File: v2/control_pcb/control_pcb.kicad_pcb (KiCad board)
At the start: 2 copper layers, 177 x 105.5 mm, 72 parts, among them J1 Raspberry_Pi_2_3, J10 8P8C_Shielded, J11 Screw_Terminal_01x02, J12 Screw_Terminal_01x02, J13 Screw_Terminal_01x02, J14 Conn_02x02_Top_Bottom, J15 Conn_02x02_Top_Bottom, J2 8P8C_Shielded, J3 Conn_01x08, J4 Conn_01x08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

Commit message: Doing more things
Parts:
- removed R20: 4k, Resistor_THT:R_Axial_DIN0207_L6.3mm_D2.5mm_P10.16mm_Horizontal
- removed U8: LM404C30ILPR, Package_TO_SOT_THT:TO-92_Inline
- added C7: 0.1uF, Capacitor_THT:C_Rect_L4.6mm_W2.0mm_P2.50mm_MKS02_FKP02, F.Cu at (120.5, 108.2)
- added G***: LOGO, LOGO, F.Cu at (173.5, 100.0)
- added R24: 10kR, Resistor_THT:R_Axial_DIN0207_L6.3mm_D2.5mm_P10.16mm_Horizontal, F.Cu at (138.1, 124.5)
- added R25: 10kR, Resistor_THT:R_Axial_DIN0207_L6.3mm_D2.5mm_P10.16mm_Horizontal, F.Cu at (138.1, 121.5)
- R17: value 904R -> 4k
- U9: value ~ -> ADS7138IRTER
- moved R23 319.3 mm to (228.0, 77.4), turned to -90 degrees
- moved H4 316.1 mm to (236.0, 33.0)
- moved H3 315.7 mm to (236.0, 129.0)
- moved R22 314.3 mm to (225.0, 87.6), turned to 90 degrees
- moved R19 305.7 mm to (218.5, 99.6), turned to 90 degrees
- moved U9 303.5 mm to (216.1, 81.6)
- moved R21 303.2 mm to (215.0, 89.4), turned to -90 degrees
- moved R18 298.9 mm to (211.6, 89.4), turned to -90 degrees
- moved R17 279.3 mm to (208.0, 99.6), turned to 90 degrees
- moved J4 252.2 mm to (228.7, 31.0), turned to -90 degrees
- moved C11 243.6 mm to (215.0, 38.5), turned to 180 degrees
- moved C12 242.2 mm to (214.8, 46.5), turned to 180 degrees
- moved C6 240.4 mm to (220.5, 80.8), turned to -90 degrees
- moved C2 232.5 mm to (204.5, 58.5), turned to 90 degrees
- moved C3 189.5 mm to (118.0, 114.8)
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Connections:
- C5 pad 1: +3.3V -> 3V3_PICO
- R17 pad 1: +5V -> +24V
- R17 pad 2: Net-(U3-VREF) -> Net-(U9-AIN6)
- R18 pad 1: +5V -> Net-(U9-AIN6)
- R18 pad 2: Net-(U9-AIN4) -> GND
- U10 pad 1: +5V -> +12V
- U10 pad 2: +5V -> +12V
- U11 pad 1: +12V -> +5V
- U11 pad 2: +12V -> +5V
- U3 pad 35: Net-(U3-VREF) -> unconnected-(U3-VREF-Pad35)
- U6 pad 1: +5V -> +12V
- U6 pad 2: +5V -> +12V
- U7 pad 1: +12V -> +5V
- U7 pad 2: +12V -> +5V
- U9 pad 3: Net-(U9-AIN4) -> +5V
- U9 pad 5: unconnected-(U9-AIN6-Pad5) -> Net-(U9-AIN6)
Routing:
- net +24V: track 0.00 -> 288.1 mm, vias 0 -> 46
- net LIMIT_SW_RR: track 0.00 -> 259.1 mm, vias 0 -> 6
- net LIMIT_SW_RL: track 0.00 -> 246.9 mm, vias 0 -> 3
- net Net-(J9-Pin_7): track 0.00 -> 213.7 mm
- net +12V: track 0.00 -> 208.0 mm, vias 0 -> 20
- net SDA: track 0.00 -> 207.3 mm, vias 0 -> 4
- net SCL: track 0.00 -> 205.6 mm, vias 0 -> 4
- net Net-(J9-Pin_5): track 0.00 -> 204.2 mm
- net Net-(J9-Pin_3): track 0.00 -> 194.8 mm
- net Net-(J9-Pin_1): track 0.00 -> 185.3 mm
- net Net-(U7-VOUT): track 0.00 -> 164.3 mm, vias 0 -> 4
- net Net-(U6-VOUT): track 0.00 -> 164.0 mm, vias 0 -> 4
- net +5V: track 3.00 -> 150.6 mm, vias 0 -> 34
- net LED1: track 0.00 -> 94.9 mm, vias 0 -> 2
- net LED2: track 0.00 -> 85.7 mm, vias 0 -> 2
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- added copper zone on B.Cu, net +12V
- added copper zone on F.Cu, net +12V
- added copper zone on B.Cu, net +24V
- added copper zone on F.Cu, net +24V
- added copper zone on F.Cu, net +5V
- added copper zone on B.Cu, net GND
- added copper zone on F.Cu, net GND
- added copper zone on F.Cu, net Net-(J14-Pin_3)
- added copper zone on F.Cu, net Net-(J14-Pin_4)
- added copper zone on F.Cu, net Net-(J15-Pin_3)
- added copper zone on F.Cu, net Net-(J15-Pin_4)
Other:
- board size 177 x 105.5 mm -> 177 x 106 mm
- board text added: "+12V"
- board text added: "+24V"
- board text added: "+5V"
- board text added: "-"
- board text added: "24V"
- board text added: "ALARM+"
- board text added: "ALARM-"
- board text added: "BOT-HOVEN"
- board text added: "CONTROL PCB VERSION 2"
- board text added: "DESIGNED BY J. PETERSEN"
- board text added: "DIR+"
- board text added: "DIR-"
- board text added: "DSCL+"
- board text added: "DSCL-"
- board text added: "DSDA+"
- board text added: "DSDA-"
- board text added: "ENA+"
- board text added: "ENA-"
- board text added: "GND"
- board text added: "J. PETERSEN A. POTENZA A. ZAKY"
- board text added: "PUL+"
- board text added: "RASPBERRY PI PICO"
- board text added: "SCL"
- board text added: "SDA"
- board text added: "T. DOBROWNEY E. EVANIUK C. KOLASKI"
- board text added: "|-GND-|"

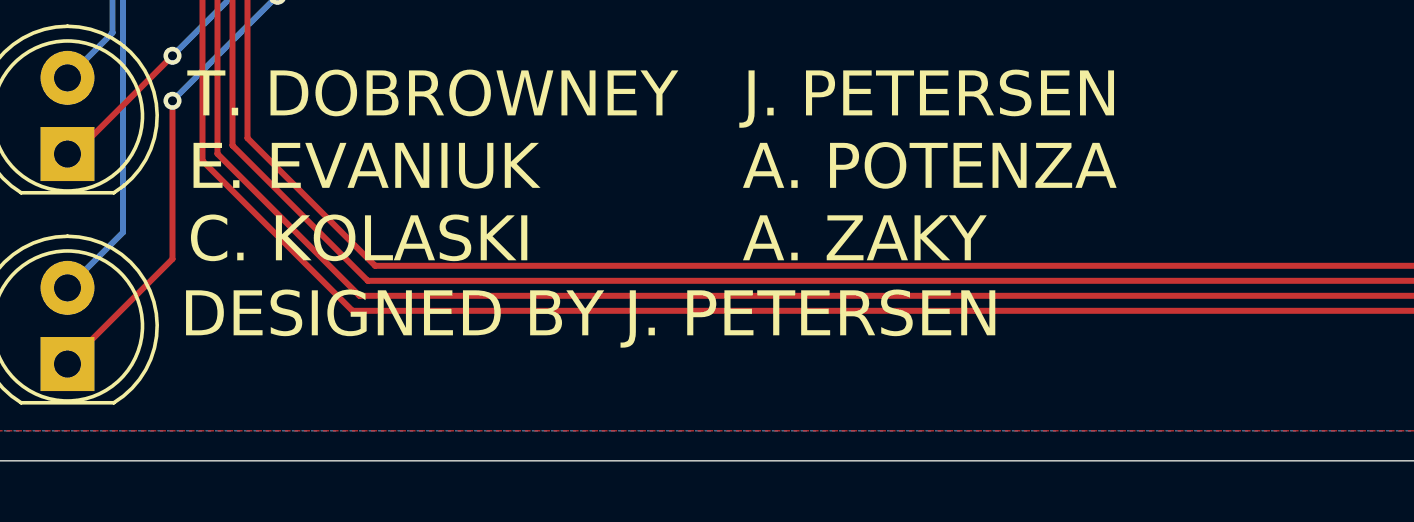
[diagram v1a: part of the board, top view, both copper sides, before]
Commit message: Version 2 As-Ordered commit
Minor changes to polish things up.
Version 2 is a major revision from the last revision, version 1. There are now 10 servo channels in addition to the 5 solenoid channels, and ADC feedback for those servos.
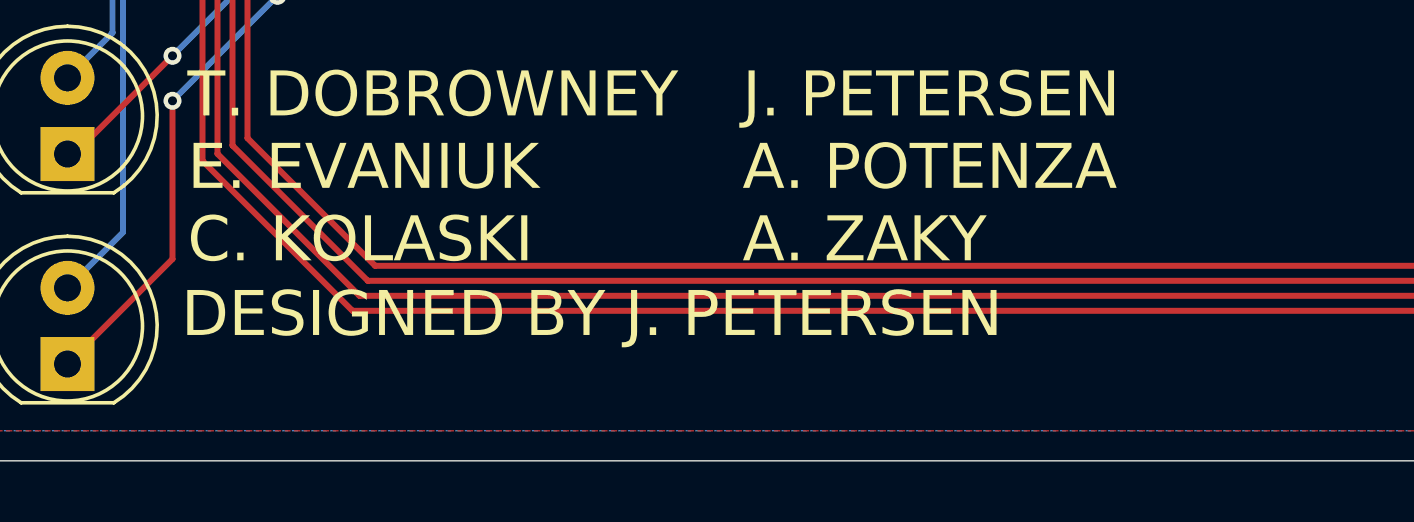
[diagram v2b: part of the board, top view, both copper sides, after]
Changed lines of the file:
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@@
 		(tags "C Rect series Radial pin pitch 2.50mm  length 4.6mm width 2mm Capacitor")
 		(property "Reference" "C12"
-			(at 1.25 2 360)
+			(at 1.25 2 0)
 			(layer "F.SilkS")
 			(effects
@@
 		)
 		(property "Value" "0.1uF"
-			(at 1.25 2.25 360)
+			(at 1.25 2.25 0)
 			(layer "F.Fab")
 			(effects
@@
 		)
 		(fp_text user "${REFERENCE}"
-			(at 1.25 0 360)
+			(at 1.25 0 0)
 			(layer "F.Fab")
 			(effects
@@
 		(tags "Resistor Axial_DIN0207 series Axial Horizontal pin pitch 10.16mm 0.25W = 1/4W length 6.3mm diameter 2.5mm")
 		(property "Reference" "R15"
-			(at 5.08 0 360)
+			(at 5.08 0 0)
 			(layer "F.SilkS")
 			(effects
@@
 		)
 		(property "Value" "504R"
-			(at 5.08 2.37 360)
+			(at 5.08 2.37 0)
 			(layer "F.Fab")
 			(effects
@@
 		)
 		(fp_text user "${REFERENCE}"
-			(at 5.08 0 360)
+			(at 5.08 0 0)
 			(layer "F.Fab")
 			(effects
@@
 		(tags "C Rect series Radial pin pitch 2.50mm  length 4.6mm width 2mm Capacitor")
 		(property "Reference" "C4"
-			(at -0.25 -2 360)
+			(at -0.25 -2 0)
 			(layer "F.SilkS")
 			(effects
@@
 		)
 		(property "Value" "0.1uF"
-			(at 1.25 2.25 360)
+			(at 1.25 2.25 0)
 			(layer "F.Fab")
 			(effects
@@
 		)
 		(fp_text user "${REFERENCE}"
-			(at 1.25 0 360)
+			(at 1.25 0 0)
 			(layer "F.Fab")
 			(effects
@@
 		)
 		(property "Value" "TCA9509DGKR"
-			(at 0 2.45 360)
+			(at 0 2.45 0)
 			(layer "F.Fab")
 			(effects
@@
 		)
 		(property "Footprint" "Package_SO:VSSOP-8_3x3mm_P0.65mm"
-			(at 0 0 360)
+			(at 0 0 0)
 			(layer "F.Fab")
 			(hide yes)
@@
 		)
 		(property "Datasheet" "https://www.ti.com/lit/ds/symlink/tca9509.pdf"
-			(at 0 0 360)
+			(at 0 0 0)
 			(layer "F.Fab")
 			(hide yes)
@@
 		)
 		(property "Description" "Level-Translating I2C Bus Buffer/Repeater, VSSOP-8"
-			(at 0 0 360)
+			(at 0 0 0)
 			(layer "F.Fab")
 			(hide yes)
@@
 		)
 		(fp_text user "${REFERENCE}"
-			(at 0 0 360)
+			(at 0 0 0)
 			(layer "F.Fab")
 			(effects
@@
 		)
 		(fp_text user "${REFERENCE}"
-			(at 0 8.89 360)
+			(at 0 8.89 0)
 			(layer "F.Fab")
 			(effects
@@
 		(tags "C Rect series Radial pin pitch 2.50mm  length 4.6mm width 2mm Capacitor")
 		(property "Reference" "C5"
-			(at 1.38785 1.906769 360)
+			(at 1.38785 1.906769 0)
 			(layer "F.SilkS")
 			(effects
@@
 		)
 		(property "Value" "0.1uF"
-			(at 1.25 2.25 360)
+			(at 1.25 2.25 0)
 			(layer "F.Fab")
 			(effects
@@
 		)
 		(fp_text user "${REFERENCE}"
-			(at 1.25 0 360)
+			(at 1.25 0 0)
 			(layer "F.Fab")
 			(effects
@@
 		(tags "Resistor Axial_DIN0207 series Axial Horizontal pin pitch 10.16mm 0.25W = 1/4W length 6.3mm diameter 2.5mm")
 		(property "Reference" "R25"
-			(at 5.08 0 360)
+			(at 5.08 0 0)
 			(layer "F.SilkS")
 			(effects
@@
 		)
 		(property "Value" "10kR"
-			(at 5.08 2.37 360)
+			(at 5.08 2.37 0)
 			(layer "F.Fab")
 			(effects
@@
 		)
 		(fp_text user "${REFERENCE}"
-			(at 5.08 0 360)
+			(at 5.08 0 0)
 			(layer "F.Fab")
 			(effects
@@
 		(tags "C Rect series Radial pin pitch 2.50mm  length 4.6mm width 2mm Capacitor")
 		(property "Reference" "C11"
-			(at 1.25 2 360)
+			(at 1.25 2 0)
 			(layer "F.SilkS")
 			(effects
@@
 		)
 		(property "Value" "0.1uF"
-			(at 1.25 2.25 360)
+			(at 1.25 2.25 0)
 			(layer "F.Fab")
 			(effects
@@
 		)
 		(fp_text user "${REFERENCE}"
-			(at 1.25 0 360)
+			(at 1.25 0 0)
 			(layer "F.Fab")
 			(effects
@@
 		(tags "Resistor Axial_DIN0207 series Axial Horizontal pin pitch 10.16mm 0.25W = 1/4W length 6.3mm diameter 2.5mm")
 		(property "Reference" "R24"
-			(at 5.08 0 360)
+			(at 5.08 0 0)
 			(layer "F.SilkS")
 			(effects
@@
 		)
 		(property "Value" "10kR"
-			(at 5.08 2.37 360)
+			(at 5.08 2.37 0)
 			(layer "F.Fab")
 			(effects
@@
 		)
 		(fp_text user "${REFERENCE}"
-			(at 5.08 0 360)
+			(at 5.08 0 0)
 			(layer "F.Fab")
 			(effects
@@
 		(tags "Resistor Axial_DIN0207 series Axial Horizontal pin pitch 10.16mm 0.25W = 1/4W length 6.3mm diameter 2.5mm")
 		(property "Reference" "R16"
-			(at 5.08 0 360)
+			(at 5.08 0 0)
 			(layer "F.SilkS")
 			(effects
@@
 		)
 		(property "Value" "504R"
-			(at 5.08 2.37 360)
+			(at 5.08 2.37 0)
 			(layer "F.Fab")
 			(effects
@@
 		)
 		(fp_text user "${REFERENCE}"
-			(at 5.08 0 360)
+			(at 5.08 0 0)
 			(layer "F.Fab")
 			(effects
@@
 		)
 		(fp_text user "${REFERENCE}"
-			(at 0 2.54 360)
+			(at 0 2.54 0)
 			(layer "F.Fab")
 			(effects
@@
 		)
 		(fp_text user "${REFERENCE}"
-			(at 0 8.89 360)
+			(at 0 8.89 0)
 			(layer "F.Fab")
 			(effects
@@
 		(tags "C Rect series Radial pin pitch 2.50mm  length 4.6mm width 2mm Capacitor")
 		(property "Reference" "C7"
-			(at 1.25 2 360)
+			(at 1.25 2 0)
 			(layer "F.SilkS")
 			(effects
@@
 		)
 		(property "Value" "0.1uF"
-			(at 1.25 2.25 360)
+			(at 1.25 2.25 0)
 			(layer "F.Fab")
 			(effects
@@
 		)
 		(fp_text user "${REFERENCE}"
-			(at 1.25 0 360)
+			(at 1.25 0 0)
 			(layer "F.Fab")
 			(effects
@@
 	)
 	(gr_text "DESIGNED BY J. PETERSEN"
-		(at 81.75 130 0)
+		(at 81.791665 129.988992 0)
 		(layer "F.SilkS" knockout)
 		(effects
@@
 		(layer "F.Cu")
 		(hatch edge 0.5)
-		(priority 9)
 		(connect_pads
 			(clearance 0.5)
@@
 		(layer "F.Cu")
 		(hatch edge 0.5)
-		(priority 3)
+		(priority 2)
 		(connect_pads yes
 			(clearance 0.5)
